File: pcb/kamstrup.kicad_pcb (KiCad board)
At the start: 2 copper layers, 26 x 26 mm, 11 parts, among them P1 CONN_4, Q1 BC557, Q2 BC547, Q3 BC547

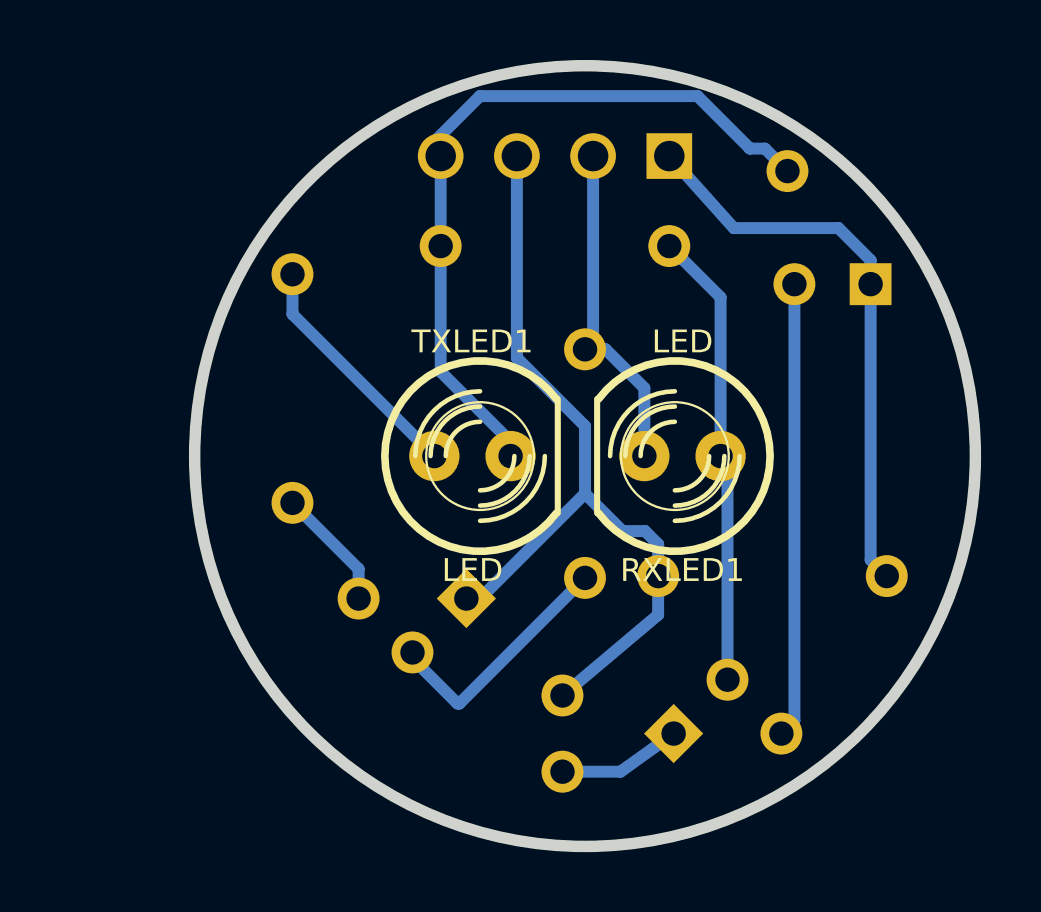
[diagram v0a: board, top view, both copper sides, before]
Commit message: SMD version first commit
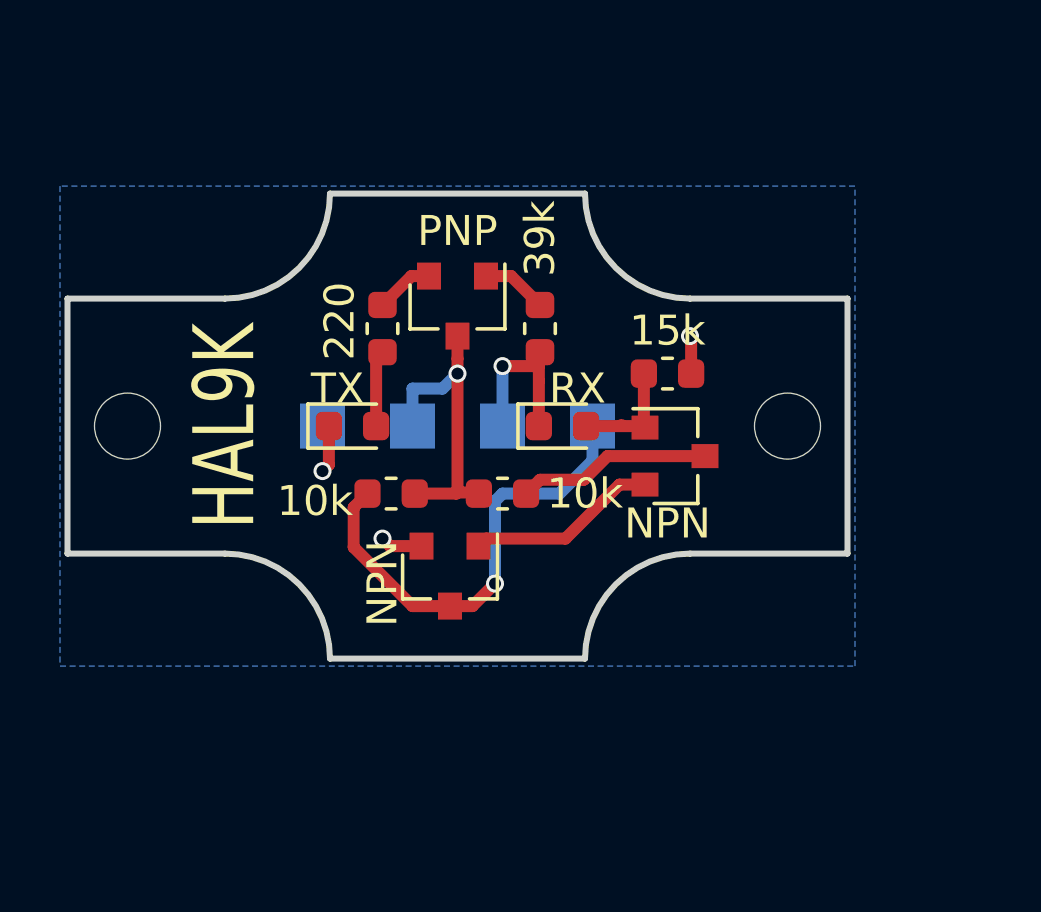
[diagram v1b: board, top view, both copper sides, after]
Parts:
- removed P1: CONN_4, PIN_ARRAY_4x1
- removed RXLED1, TXLED1: LED, LED-5MM
- added D1: TX, LED_SMD:LED_0603_1608Metric, F.Cu at (41.5, 45.0)
- added D2: RX, LED_SMD:LED_0603_1608Metric, F.Cu at (48.5, 45.0)
- added H1: MountingHole, MountingHole:MountingHole_2.2mm_M2, F.Cu at (34.0, 45.0)
- added H2: MountingHole, MountingHole:MountingHole_2.2mm_M2, F.Cu at (56.0, 45.0)
- added J1: GND, TestPoint:TestPoint_Pad_1.5x1.5mm, B.Cu at (40.5, 45.0)
- added J2: 5V, TestPoint:TestPoint_Pad_1.5x1.5mm, B.Cu at (43.5, 45.0)
- added J3: TX, TestPoint:TestPoint_Pad_1.5x1.5mm, B.Cu at (46.5, 45.0)
- added J4: RX, TestPoint:TestPoint_Pad_1.5x1.5mm, B.Cu at (49.5, 45.0)
- Q1: value BC557 -> PNP; footprint TO92-123 -> Package_TO_SOT_SMD:SOT-23; moved to F.Cu
- Q2, Q3: value BC547 -> NPN; footprint TO92 -> Package_TO_SOT_SMD:SOT-23; moved to F.Cu
- R1, R2, R3, R5: footprint R3 -> Resistor_SMD:R_0603_1608Metric; moved to F.Cu
- R4: footprint R1 -> Resistor_SMD:R_0603_1608Metric; moved to F.Cu
- moved Q3 16.8 mm to (44.8, 50.0), turned to 270 degrees
- moved R5 13.0 mm to (42.8, 47.2), turned to 0 degrees
- moved Q1 9.86 mm to (45.0, 41.0), turned to 270 degrees
- moved Q2 9.41 mm to (52.2, 46.0), turned to 0 degrees
- moved R4 8.25 mm to (46.5, 47.2), turned to 180 degrees
- moved R3 5.67 mm to (52.0, 43.2), turned to 180 degrees
- moved R1 4.74 mm to (47.8, 41.8), turned to 90 degrees
- moved R2 3.61 mm to (42.5, 41.8), turned to 270 degrees
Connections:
- net +3.3V renamed +5V
- Q1 pad 1: N-000007 -> Net-(Q1-Pad1)
- Q1 pad 2: N-000005 -> Net-(Q1-Pad2)
- Q2 pad 1: N-000002 -> Net-(D2-Pad2)
- Q2 pad 2: N-000010 -> Net-(Q2-Pad2)
- Q2 pad 3: N-000001 -> Net-(Q2-Pad3)
- Q3 pad 1: RX -> Net-(Q2-Pad2)
- Q3 pad 2: N-000001 -> GND
- Q3 pad 3: GND -> RX
- R1 pad 2: N-000005 -> Net-(Q1-Pad1)
- R2 pad 1: N-000007 -> Net-(Q1-Pad2)
- R3 pad 2: N-000010 -> Net-(D2-Pad2)
- R4 pad 1: N-000002 -> Net-(Q2-Pad3)
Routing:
- net GND: track 25.0 -> 4.26 mm, vias 0 -> 3
- net +5V: track 27.3 -> 10.3 mm, vias 0 -> 1
- net N-000010: track 15.3 -> 0.00 mm
- net N-000001: track 15.2 -> 0.00 mm
- net N-000005: track 8.31 -> 0.00 mm
- net Net-(Q2-Pad3): track 0.00 -> 6.48 mm
- net Net-(Q2-Pad2): track 0.00 -> 6.40 mm
- net TX: track 11.3 -> 5.69 mm, vias 0 -> 1
- net Net-(D1-Pad2): track 8.02 -> 2.55 mm
- net N-000002: track 4.11 -> 0.00 mm
- net N-000007: track 4.10 -> 0.00 mm
- net Net-(D2-Pad2): track 0.00 -> 3.85 mm
- net RX: track 19.0 -> 15.5 mm, vias 0 -> 1
- net Net-(Q1-Pad1): track 0.00 -> 2.20 mm
- net Net-(Q1-Pad2): track 0.00 -> 1.95 mm
- added copper zone on B.Cu, net GND
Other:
- board size 26 x 26 mm -> 26 x 15.5 mm
- net class Default: trace_width 0.39878 -> 0.2; via_dia 0.889 -> 0.6; via_drill 0.635 -> 0.4
- rule trace_min: 0.39878 -> 0.2
- rule via_min_drill: 0.508 -> 0.3
- rule via_min_size: 0.889 -> 0.6
- board text added: "Designed By: AndersV209"
- board text added: "HAL9K"
- board text added: "IR-EYE"
